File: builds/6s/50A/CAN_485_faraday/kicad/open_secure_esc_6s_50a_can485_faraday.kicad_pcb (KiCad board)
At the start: 4 copper layers, 32 x 60.1 mm, 59 parts, among them J1 SolderPad_1x04_SMD_P1.27mm_Pr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, J2 SolderPad_1x02_SMD_P2.54mm, J3 SolderPad_1x02_SMD_P2.54mm, J4A SolderWirePad_1x01_SMD_5x10mm, J4B SolderWirePad_1x01_SMD_5x10mm, J4C SolderWirePad_1x01_SMD_5x10mm, J5A SolderWire-6sqmm_1x01_D3.5mm_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, J5B SolderWire-6sqmm_1x01_D3.5mm_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, Q1 Toshiba_2-5W1A_SOP-Advance-N_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, Q2 Toshiba_2-5W1A_SOP-Advance-N_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, Q3 Toshiba_2-5W1A_SOP-Advance-N_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, Q4 Toshiba_2-5W1A_SOP-Advance-N_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, Q5 Toshiba_2-5W1A_SOP-Advance-N_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, Q6 Toshiba_2-5W1A_SOP-Advance-N_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, U1 LQFP-64_10x10mm_P0.5mm, U2 Infineon_PG-USON-10-2-4_3x3mm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, U3 SOIC-20W_7.5x12.8mm_P1.27mm, U4 SOIC-20W_7.5x12.8mm_P1.27mm, U5 TI_RTA0040B_WQFN-40_6x6mm_P0.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, U6 SOIC-8_3.9x4.9mm_P1.27mm, U7 SOIC-8_3.9x4.9mm_P1.27mm, U8 SOIC-8_3.9x4.9mm_P1.27mm

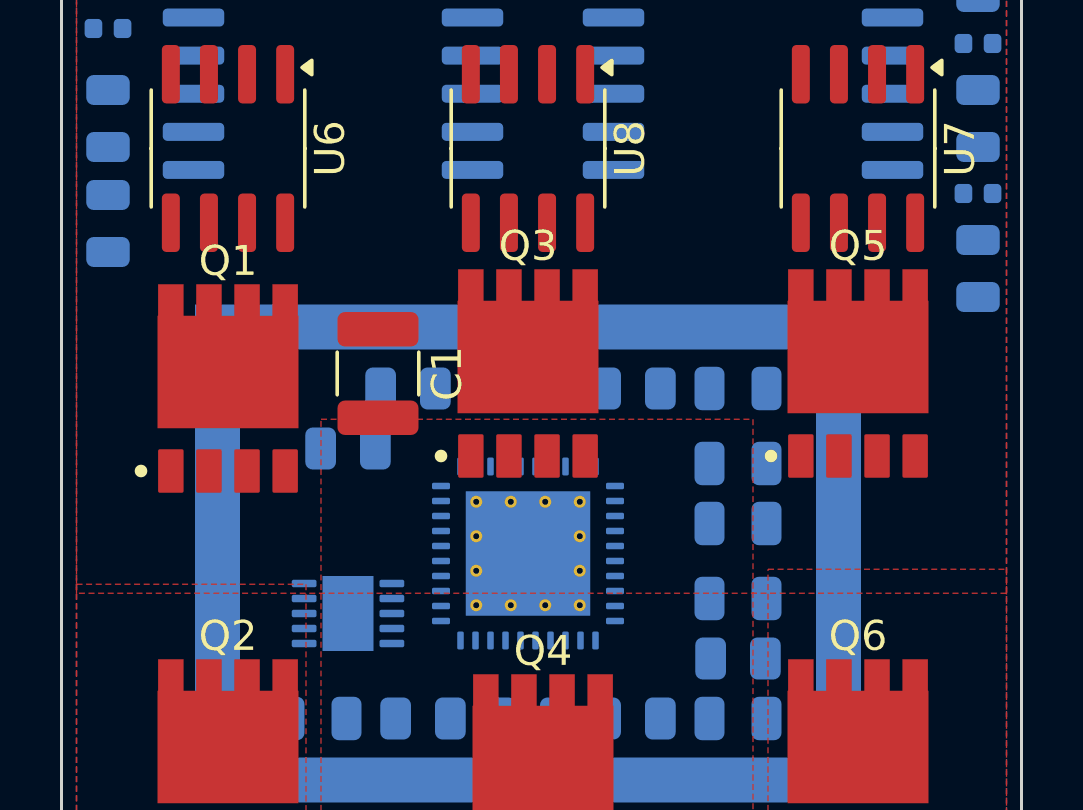
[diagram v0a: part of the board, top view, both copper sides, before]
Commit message: Fix a bug in my own creepage harness: it measured centres, not edges
The harness compared pad CENTRES. Creepage and clearance are defined between
the nearest points of two conductors -- edge to edge. Centre-to-centre
overstates the gap by roughly half a pad on each side, which on a 7.5 mm
requirement is the entire margin.

Every creepage number reported from this harness was therefore optimistic,
including the "7.68 mm, PASSES" result attributed to the U1/U5 swap. Corrected:

    pair                    edge-to-edge    centre-to-centre (wrong)
    C14.2 <-> SH1.1              2.51 mm            10.69 mm
    U4.11 <-> J5B.1              2.80 mm             8.60 mm
    C18.1 <-> SH1.1              3.18 mm             9.73 mm
    U3.20 <-> J5A.1              3.28 mm             9.02 mm

The board fails creepage by 5 mm, not passes by 0.18. The swap's other gains
stand -- gate loop 22.32 -> 16.83 mm is a centre-to-centre measure between pad
centres on the same net, where centres are the right thing to compare.

THE ERROR HID THE BIGGEST OFFENDER. SH1, the WE-SHC shield frame, is a GND
conductor with a 22.2 x 16.6 mm perimeter running alongside both isolated
support columns. Its CENTRE is far from everything on the board; its EDGE is
2.51 mm from C14. A centre-based measure cannot see a large ring at all, so
the shield never appeared in any ranking until now. It is the single worst
creepage offender on the board and had been invisible for the whole session.

Also corrected by the same fix: commutation_max_mm reads 19.60 mm rather than
17.41, since that too was being measured centre-to-centre.

Harness now carries the bbox on every pad record and compares axis-aligned
box gaps. The docstring records why, so the next reader does not revert it.

Co-Authored-By: Claude Opus 5 <noreply@anthropic.com>
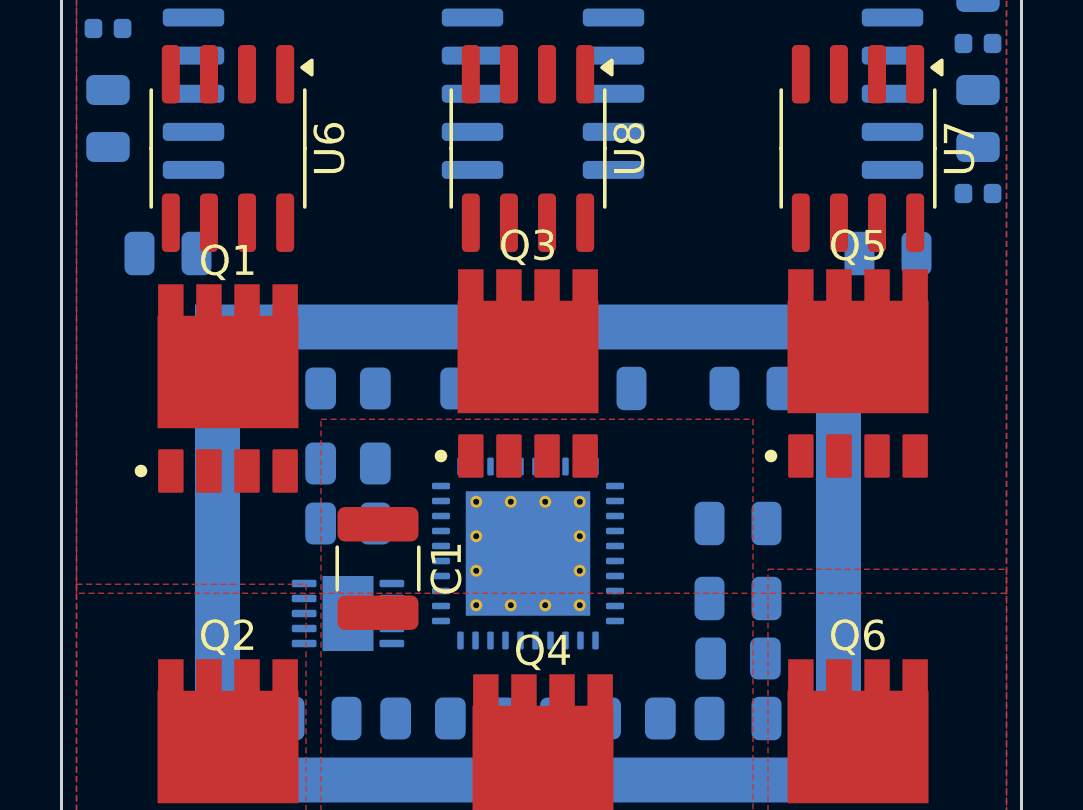
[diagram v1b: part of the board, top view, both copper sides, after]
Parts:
- moved C1 6.50 mm to (30.5, 53.5)
- moved R9 5.50 mm to (29.5, 47.5)
- moved C2 5.15 mm to (38.0, 47.5)
- moved R6 5.00 mm to (34.0, 47.5)
- moved R11 3.20 mm to (29.5, 50.0)
- moved C18 3.04 mm to (47.5, 43.0), turned to 0 degrees
- moved R14 2.50 mm to (29.5, 52.0)
- moved C14 2.24 mm to (23.5, 43.0), turned to 0 degrees
- moved C8 0.50 mm to (43.0, 47.5)
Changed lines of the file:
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@@
 	(footprint "C_1210_3225Metric"
 		(layer "F.Cu")
-		(at 30.5 47 -90)
+		(at 30.5 53.5 -90)
 		(descr "Capacitor SMD 1210 (3225 Metric), square (rectangular) end terminal, IPC-7351 nominal, (Body size source: IPC-SM-782 page 76, https://www.pcb-3d.com/wordpress/wp-content/uploads/ipc-sm-782a_amendment_1_and_2.pdf), generated with kicad-footprint-generator")
 		(tags "capacitor")
@@
 	(footprint "R_0805_2012Metric"
 		(layer "B.Cu")
-		(at 31.5 47.5 180)
+		(at 29.5 50 180)
 		(descr "Resistor SMD 0805 (2012 Metric), square (rectangular) end terminal, IPC-7351 nominal, (Body size source: IPC-SM-782 page 72, https://www.pcb-3d.com/wordpress/wp-content/uploads/ipc-sm-782a_amendment_1_and_2.pdf), generated with kicad-footprint-generator")
 		(tags "resistor")
@@
 	(footprint "R_0805_2012Metric"
 		(layer "B.Cu")
-		(at 39 47.5 180)
+		(at 34 47.5 180)
 		(descr "Resistor SMD 0805 (2012 Metric), square (rectangular) end terminal, IPC-7351 nominal, (Body size source: IPC-SM-782 page 72, https://www.pcb-3d.com/wordpress/wp-content/uploads/ipc-sm-782a_amendment_1_and_2.pdf), generated with kicad-footprint-generator")
 		(tags "resistor")
@@
 	(footprint "R_0805_2012Metric"
 		(layer "B.Cu")
-		(at 35 47.5 180)
+		(at 29.5 47.5 180)
 		(descr "Resistor SMD 0805 (2012 Metric), square (rectangular) end terminal, IPC-7351 nominal, (Body size source: IPC-SM-782 page 72, https://www.pcb-3d.com/wordpress/wp-content/uploads/ipc-sm-782a_amendment_1_and_2.pdf), generated with kicad-footprint-generator")
 		(tags "resistor")
@@
 	(footprint "C_0805_2012Metric"
 		(layer "B.Cu")
-		(at 42.5 50 180)
+		(at 38 47.5 180)
 		(descr "Capacitor SMD 0805 (2012 Metric), square (rectangular) end terminal, IPC-7351 nominal, (Body size source: IPC-SM-782 page 76, https://www.pcb-3d.com/wordpress/wp-content/uploads/ipc-sm-782a_amendment_1_and_2.pdf, https://docs.google.com/spreadsheets/d/1BsfQQcO9C6DZCsRaXUlFlo91Tg2WpOkGARC1WS5S8t0/edit?usp=sharing), generated with kicad-footprint-generator")
 		(tags "capacitor")
@@
 	(footprint "C_0805_2012Metric"
 		(layer "B.Cu")
-		(at 21.5 42 -90)
+		(at 23.5 43)
 		(descr "Capacitor SMD 0805 (2012 Metric), square (rectangular) end terminal, IPC-7351 nominal, (Body size source: IPC-SM-782 page 76, https://www.pcb-3d.com/wordpress/wp-content/uploads/ipc-sm-782a_amendment_1_and_2.pdf, https://docs.google.com/spreadsheets/d/1BsfQQcO9C6DZCsRaXUlFlo91Tg2WpOkGARC1WS5S8t0/edit?usp=sharing), generated with kicad-footprint-generator")
 		(tags "capacitor")
 		(property "Reference" "C14"
-			(at 0 1.68 90)
+			(at 0 1.68 0)
 			(layer "B.SilkS")
 			(effects
@@
 		)
 		(property "Value" "10nF"
-			(at 0 -1.68 90)
+			(at 0 -1.68 0)
 			(layer "B.Fab")
 			(effects
@@
 		)
 		(property "Datasheet" ""
-			(at 0 0 90)
+			(at 0 0 0)
 			(layer "B.Fab")
 			(hide yes)
@@
 		)
 		(property "Description" ""
-			(at 0 0 90)
+			(at 0 0 0)
 			(layer "B.Fab")
 			(hide yes)
@@
 		(attr smd)
 		(fp_line
-			(start -0.261252 0.735)
-			(end 0.261252 0.735)
+			(start -0.261252 -0.735)
+			(end 0.261252 -0.735)
 			(stroke
 				(width 0.12)
@@
 		)
 		(fp_line
-			(start -0.261252 -0.735)
-			(end 0.261252 -0.735)
+			(start -0.261252 0.735)
+			(end 0.261252 0.735)
 			(stroke
 				(width 0.12)
@@
 		)
 		(fp_line
-			(start -1.7 0.98)
-			(end 1.7 0.98)
+			(start -1.7 -0.98)
+			(end -1.7 0.98)
 			(stroke
 				(width 0.05)
@@
 		)
 		(fp_line
-			(start 1.7 0.98)
-			(end 1.7 -0.98)
+			(start -1.7 0.98)
+			(end 1.7 0.98)
 			(stroke
 				(width 0.05)
@@
 		)
 		(fp_line
-			(start -1.7 -0.98)
-			(end -1.7 0.98)
+			(start 1.7 -0.98)
+			(end -1.7 -0.98)
 			(stroke
 				(width 0.05)
@@
 		)
 		(fp_line
-			(start 1.7 -0.98)
-			(end -1.7 -0.98)
+			(start 1.7 0.98)
+			(end 1.7 -0.98)
 			(stroke
 				(width 0.05)
@@
 		)
 		(fp_line
-			(start -1 0.625)
-			(end 1 0.625)
+			(start -1 -0.625)
+			(end -1 0.625)
 			(stroke
 				(width 0.1)
@@
 		)
 		(fp_line
-			(start 1 0.625)
-			(end 1 -0.625)
+			(start -1 0.625)
+			(end 1 0.625)
 			(stroke
 				(width 0.1)
@@
 		)
 		(fp_line
-			(start -1 -0.625)
-			(end -1 0.625)
+			(start 1 -0.625)
+			(end -1 -0.625)
 			(stroke
 				(width 0.1)
@@
 		)
 		(fp_line
-			(start 1 -0.625)
-			(end -1 -0.625)
+			(start 1 0.625)
+			(end 1 -0.625)
 			(stroke
 				(width 0.1)
@@
 		)
 		(fp_text user "${REFERENCE}"
-			(at 0 0 90)
+			(at 0 0 0)
 			(layer "B.Fab")
 			(effects
@@
 		)
 		(pad "1" smd roundrect
-			(at -0.95 0 270)
+			(at -0.95 0)
 			(size 1 1.45)
 			(layers "B.Cu" "B.Mask" "B.Paste")
@@
 		)
 		(pad "2" smd roundrect
-			(at 0.95 0 270)
+			(at 0.95 0)
 			(size 1 1.45)
 			(layers "B.Cu" "B.Mask" "B.Paste")
@@
 	(footprint "R_0805_2012Metric"
 		(layer "B.Cu")
-		(at 29.5 49.5 180)
+		(at 29.5 52 180)
 		(descr "Resistor SMD 0805 (2012 Metric), square (rectangular) end terminal, IPC-7351 nominal, (Body size source: IPC-SM-782 page 72, https://www.pcb-3d.com/wordpress/wp-content/uploads/ipc-sm-782a_amendment_1_and_2.pdf), generated with kicad-footprint-generator")
 		(tags "resistor")
@@
 	(footprint "C_0805_2012Metric"
 		(layer "B.Cu")
-		(at 50.5 43.5 90)
+		(at 47.5 43)
 		(descr "Capacitor SMD 0805 (2012 Metric), square (rectangular) end terminal, IPC-7351 nominal, (Body size source: IPC-SM-782 page 76, https://www.pcb-3d.com/wordpress/wp-content/uploads/ipc-sm-782a_amendment_1_and_2.pdf, https://docs.google.com/spreadsheets/d/1BsfQQcO9C6DZCsRaXUlFlo91Tg2WpOkGARC1WS5S8t0/edit?usp=sharing), generated with kicad-footprint-generator")
 		(tags "capacitor")
 		(property "Reference" "C18"
-			(at 0 1.68 270)
+			(at 0 1.68 0)
 			(layer "B.SilkS")
 			(effects
@@
 		)
 		(property "Value" "10nF"
-			(at 0 -1.68 270)
+			(at 0 -1.68 0)
 			(layer "B.Fab")
 			(effects
@@
 		)
 		(property "Datasheet" ""
-			(at 0 0 270)
+			(at 0 0 0)
 			(layer "B.Fab")
 			(hide yes)
@@
 		)
 		(property "Description" ""
-			(at 0 0 270)
+			(at 0 0 0)
 			(layer "B.Fab")
 			(hide yes)
@@
 		)
 		(fp_line
-			(start 1.7 -0.98)
-			(end -1.7 -0.98)
+			(start -1.7 -0.98)
+			(end -1.7 0.98)
 			(stroke
 				(width 0.05)
@@
 		)
 		(fp_line
-			(start -1.7 -0.98)
-			(end -1.7 0.98)
+			(start -1.7 0.98)
+			(end 1.7 0.98)
 			(stroke
 				(width 0.05)
@@
 		)
 		(fp_line
-			(start 1.7 0.98)
-			(end 1.7 -0.98)
+			(start 1.7 -0.98)
+			(end -1.7 -0.98)
 			(stroke
 				(width 0.05)
@@
 		)
 		(fp_line
-			(start -1.7 0.98)
-			(end 1.7 0.98)
+			(start 1.7 0.98)
+			(end 1.7 -0.98)
 			(stroke
 				(width 0.05)
@@
 		)
 		(fp_line
-			(start 1 -0.625)
-			(end -1 -0.625)
+			(start -1 -0.625)
+			(end -1 0.625)
 			(stroke
 				(width 0.1)
@@
 		)
 		(fp_line
-			(start -1 -0.625)
-			(end -1 0.625)
+			(start -1 0.625)
+			(end 1 0.625)
 			(stroke
 				(width 0.1)
@@
 		)
 		(fp_line
-			(start 1 0.625)
-			(end 1 -0.625)
+			(start 1 -0.625)
+			(end -1 -0.625)
 			(stroke
 				(width 0.1)
@@
 		)
 		(fp_line
-			(start -1 0.625)
-			(end 1 0.625)
+			(start 1 0.625)
+			(end 1 -0.625)
 			(stroke
 				(width 0.1)
@@
 		)
 		(fp_text user "${REFERENCE}"
-			(at 0 0 270)
+			(at 0 0 0)
 			(layer "B.Fab")
 			(effects
@@
 		)
 		(pad "1" smd roundrect
-			(at -0.95 0 90)
+			(at -0.95 0)
 			(size 1 1.45)
 			(layers "B.Cu" "B.Mask" "B.Paste")
@@
 		)
 		(pad "2" smd roundrect
-			(at 0.95 0 90)
+			(at 0.95 0)
 			(size 1 1.45)
 			(layers "B.Cu" "B.Mask" "B.Paste")
@@
 	(footprint "C_0805_2012Metric"
 		(layer "B.Cu")
-		(at 42.5 47.5 180)
+		(at 43 47.5 180)
 		(descr "Capacitor SMD 0805 (2012 Metric), square (rectangular) end terminal, IPC-7351 nominal, (Body size source: IPC-SM-782 page 76, https://www.pcb-3d.com/wordpress/wp-content/uploads/ipc-sm-782a_amendment_1_and_2.pdf, https://docs.google.com/spreadsheets/d/1BsfQQcO9C6DZCsRaXUlFlo91Tg2WpOkGARC1WS5S8t0/edit?usp=sharing), generated with kicad-footprint-generator")
 		(tags "capacitor")

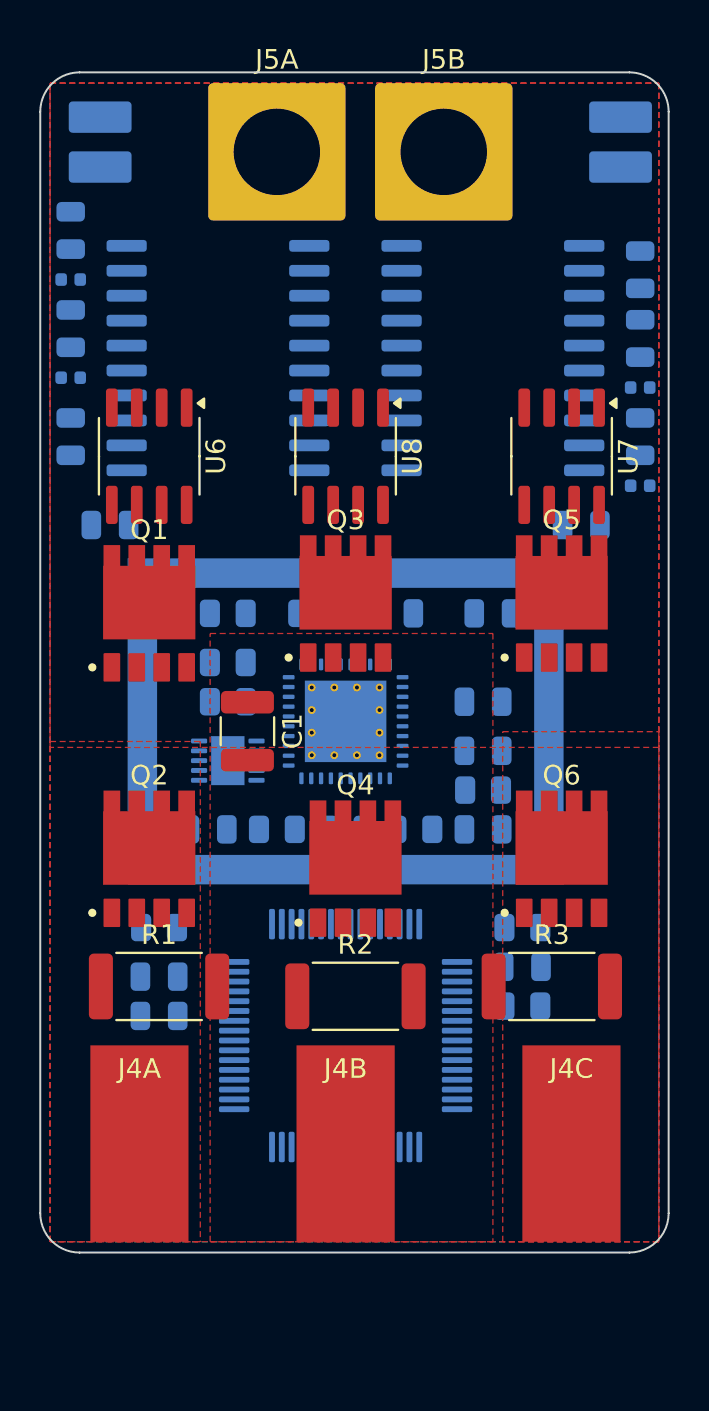
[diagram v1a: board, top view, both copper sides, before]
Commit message: Lengthen to 66.1 mm: the shield now clears the isolated section
SH1 is a GND conductor with 77.6 mm of perimeter sitting under the isolated
support columns, and it was the dominant creepage offender at 1.98 mm against
[9] Table 6's 7.5 mm. Moving the power/control block down 6.00 mm clears it:
SH1 no longer appears among the closest isolated-to-non-isolated pairs at all.

    board                32.00 x 60.10  ->  32.00 x 66.10 mm
    creepage min                  1.98  ->  2.80 mm
    binding pair          C14/C18<->SH1  ->  U4.11 <-> J5B.1
    DRC electrical                                        0
    isolated lead max                                  9.31 mm  (limit 10)
    gate loop max                                     16.49 mm

A SMALLER CAN WAS EVALUATED AND REJECTED ON THE ARITHMETIC. The can's contents
measure 16.90 x 12.45 mm and need a 13.45 mm cavity, so a ~15.2 mm-tall can
would fit -- but shrinking with the bottom fixed lifts the top edge only
1.40 mm. Lifting C14/C18 buys 2.40 more and FB4 another 0.81, after which the
next isolated conductors are U3.11/U4.20 at y 20.61 -- the transceivers' own
pins, unmovable without pushing the ICs into J2/J3 and the board edge. Every
available move totals 4.61 mm against a 5.52 mm requirement. Length was the
only lever, and the existing 3670209 stays.

TWO TRAPS FROM EARLIER ATTEMPTS AVOIDED BY DESIGN, BOTH RECORDED IN THE TOOL:

  * The moving set is named by FUNCTION, not by a y coordinate. At any
    threshold between the isolated section's bottom (23.82) and SH1's top
    (25.80), Q1/Q3/Q5 fall on the stationary side while Q2/Q4/Q6 move --
    splitting every half-bridge and destroying the commutation loop. The
    script holds the isolated block and pack terminals by name and translates
    the rest, then asserts SH1, U5, U1, Q1-Q6 and J4A/B/C actually moved.
  * Zones are classified translate-versus-extend per zone. A pour tied to
    parts that move (PH_A/B/C, GND on In2) translates with them; a plane
  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
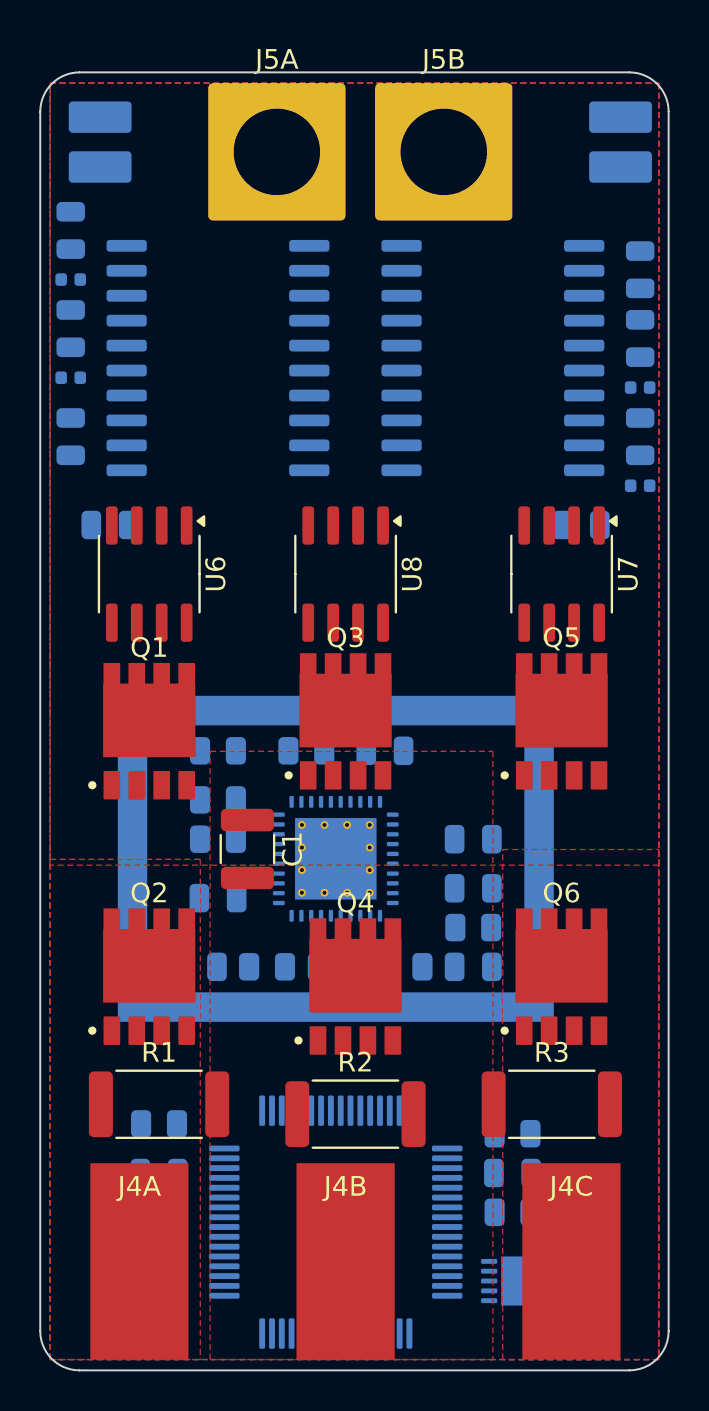
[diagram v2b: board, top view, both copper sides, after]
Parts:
- moved U2 30.3 mm to (44.3, 81.5)
- moved C8 20.2 mm to (29.0, 62.0)
- moved C10 10.5 mm to (44.0, 76.0)
- moved R12 10.5 mm to (44.0, 74.0)
- moved R8 10.5 mm to (44.0, 78.0)
- moved C3 10.0 mm to (26.0, 78.0)
- moved C4 10.0 mm to (26.0, 76.0)
- moved R7 10.0 mm to (26.0, 73.5)
- moved U1 9.51 mm to (35.0, 78.5)
- moved J1 8.56 mm to (25.0, 81.0), turned to 0 degrees
- moved C2 7.02 mm to (37.5, 54.5)
- moved C5 7.02 mm to (42.0, 59.0)
- moved C6 7.02 mm to (42.0, 61.5)
- moved C7 7.02 mm to (42.0, 65.5)
- moved C9 7.02 mm to (28.0, 65.5)
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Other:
- board size 32 x 60.1 mm -> 32 x 66.1 mm
